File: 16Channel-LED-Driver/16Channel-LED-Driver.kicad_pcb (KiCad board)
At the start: 2 copper layers, 190.5 x 80 mm, 264 parts, among them P1 CONN_01X02, P10 CONN_01X02, P11 CONN_01X02, P12 CONN_01X02, P13 CONN_01X02, P14 CONN_01X02, P2 CONN_01X06, P3 CONN_01X02, P4 CONN_01X02, P5 CONN_01X06, P6 CONN_01X08, P7 CONN_01X08, P8 CONN_01X08, P9 CONN_01X08, Q1 BC413, Q10 BC413, Q11 BUT11, Q12 BC413, Q13 BUT11, Q14 BC413, Q15 BC413, Q16 BC413, Q17 BUT11, Q18 BC413, Q19 BC413, Q2 BC413, Q20 BC413, Q21 BUT11, Q22 BC413, Q23 BUT11, Q24 BC413, Q25 BUT11, Q26 BC413, Q27 BC413, Q28 BC413, Q29 BC413, Q3 BC413, Q30 BC413, Q31 BUT11, Q32 BC413, Q33 BUT11, Q34 BC413, Q35 BC413, Q36 BUT11, Q37 BC413, Q38 BUT11, Q4 BC413, Q5 BUT11, Q51 BC413, Q52 BC413, Q55 BC413, Q56 BUT11, Q57 BC413, Q58 BUT11, Q59 BC413, Q6 BC413, Q60 BC413, Q63 BC413, Q64 BUT11, Q65 BC413, Q66 BUT11, Q7 BUT11, Q8 BC413, Q9 BC413, U1 LD3985G, U2 LD3985G, U3 PCA9634, U4 LM324AN, U5 LM324AN, U6 PCA9634, U7 LM324AN, U8 LM324AN

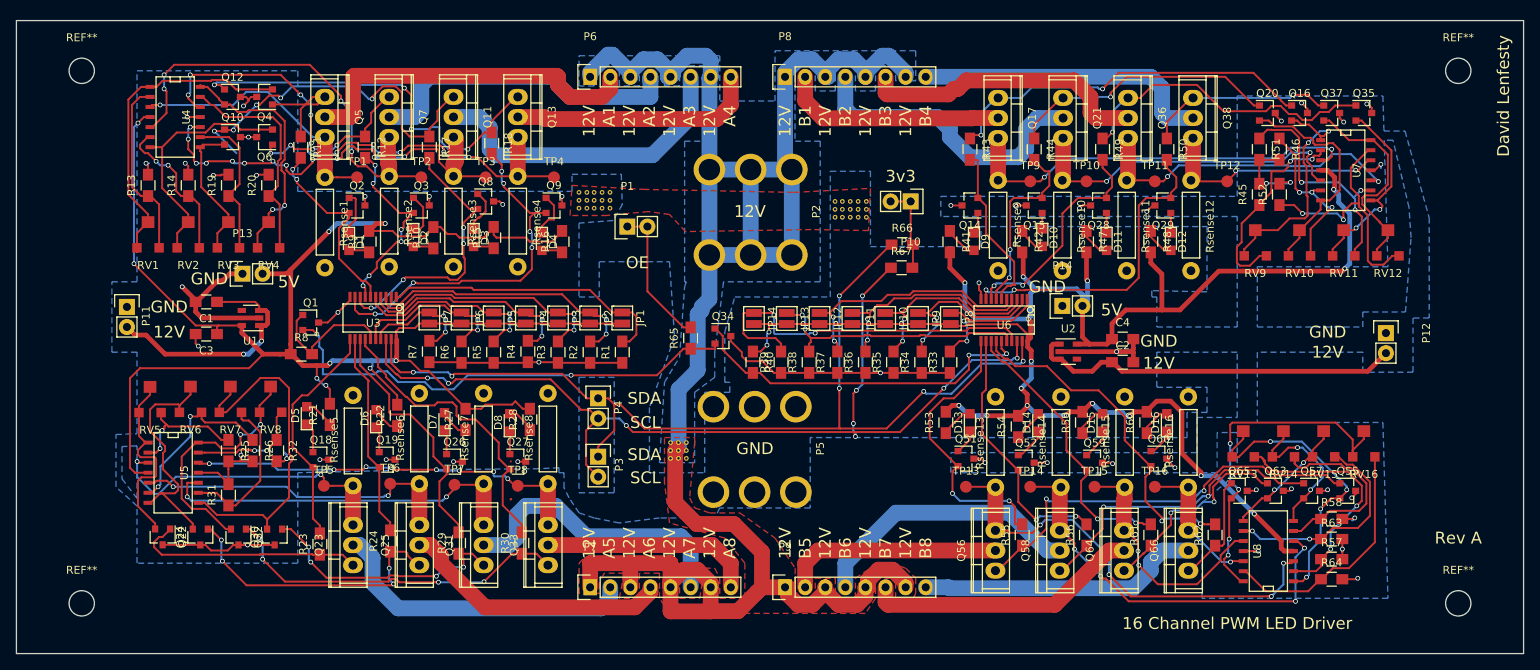
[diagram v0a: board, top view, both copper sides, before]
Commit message: Did Revision B of the 16 Channel board, also exported some gerbers
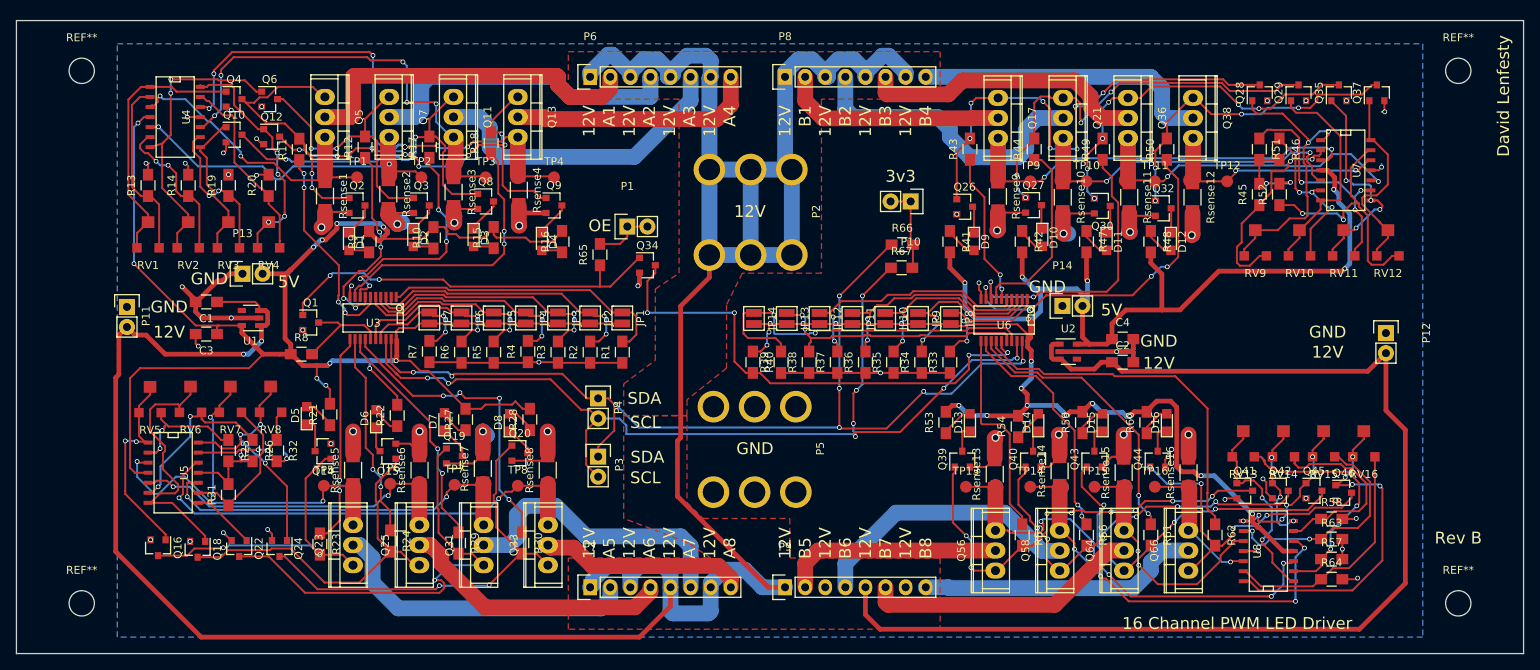
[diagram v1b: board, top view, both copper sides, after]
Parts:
- removed Q51, Q52, Q55, Q57, Q59, Q60, Q63, Q65: BC413, TO_SOT_Packages_SMD:SOT-23
- removed the REF** at (139.9, 105.4)
- removed the REF** at (138.9, 105.4)
- removed the REF** at (162.7, 76.9)
- removed the REF** at (162.7, 74.9)
- removed the REF** at (162.7, 75.9)
- removed the REF** at (161.6, 75.9)
- removed the REF** at (161.6, 76.9)
- removed the REF** at (160.6, 76.9)
- removed the REF** at (160.6, 75.9)
- removed the REF** at (158.7, 75.9)
- removed the REF** at (158.7, 76.9)
- removed the REF** at (159.6, 76.9)
- removed the REF** at (158.7, 74.9)
- removed the REF** at (159.6, 75.9)
- removed the REF** at (159.6, 74.9)
- removed the REF** at (161.6, 74.9)
- removed the REF** at (160.6, 74.9)
- removed the REF** at (126.3, 74.8)
- removed the REF** at (127.3, 75.8)
- removed the REF** at (127.3, 74.8)
- removed the REF** at (126.3, 75.8)
- removed the REF** at (126.3, 73.8)
- removed the REF** at (127.3, 73.8)
- removed the REF** at (130.3, 75.8)
- removed the REF** at (129.3, 75.8)
- removed the REF** at (128.3, 75.8)
- removed the REF** at (130.3, 74.8)
- removed the REF** at (129.3, 74.8)
- removed the REF** at (128.3, 74.8)
- removed the REF** at (130.3, 73.8)
- removed the REF** at (139.9, 107.4)
- removed the REF** at (129.3, 73.8)
- removed the REF** at (128.3, 73.8)
- removed the REF** at (137.9, 105.4)
- removed the REF** at (138.9, 107.4)
- removed the REF** at (137.9, 107.4)
- removed the REF** at (139.9, 106.4)
- removed the REF** at (138.9, 106.4)
- removed the REF** at (137.9, 106.4)
- added Q39: Q_NPN_BEC, TO_SOT_Packages_SMD:SOT-23, F.Cu at (174.8, 107.5)
- added Q40: Q_NPN_BEC, TO_SOT_Packages_SMD:SOT-23, F.Cu at (183.8, 107.5)
- added Q41: Q_NPN_BEC, TO_SOT_Packages_SMD:SOT-23, F.Cu at (210.5, 111.5)
- added Q42: Q_NPN_BEC, TO_SOT_Packages_SMD:SOT-23, F.Cu at (215.0, 111.5)
- added Q43: Q_NPN_BEC, TO_SOT_Packages_SMD:SOT-23, F.Cu at (191.5, 107.5)
- added Q44: Q_NPN_BEC, TO_SOT_Packages_SMD:SOT-23, F.Cu at (199.5, 107.5)
- added Q45: Q_NPN_BEC, TO_SOT_Packages_SMD:SOT-23, F.Cu at (219.2, 111.5)
- added Q46: Q_NPN_BEC, TO_SOT_Packages_SMD:SOT-23, F.Cu at (223.0, 111.8)
- Q1, Q10, Q12, Q14, Q15, Q16, Q18, Q19, Q2, Q20, Q22, Q24, Q26, Q27, Q28, Q29, Q3, Q30, Q32, Q34, Q35, Q37, Q4, Q6, Q8, Q9: value BC413 -> Q_NPN_BEC
- Rsense1, Rsense10, Rsense11, Rsense12, Rsense13, Rsense14, Rsense15, Rsense16, Rsense2, Rsense3, Rsense4, Rsense5, Rsense6, Rsense7, Rsense8, Rsense9: footprint Custom_Footprints:Current_Sense_Resistor -> Resistors_SMD:R_1206_HandSoldering
- moved Q16 154.4 mm to (73.2, 118.7), turned to 270 degrees
- moved Q32 124.1 mm to (200.2, 75.8), turned to 0 degrees
- moved Q30 112.7 mm to (192.5, 75.5), turned to 0 degrees
- moved Q20 103.8 mm to (118.9, 106.8)
- moved Q14 87.5 mm to (94.0, 106.5)
- moved Q15 87.4 mm to (102.2, 106.5)
- moved Q27 72.8 mm to (183.8, 75.4)
- moved Q26 72.1 mm to (175.1, 75.6)
- moved Q28 24.9 mm to (212.4, 61.2), turned to 90 degrees
- moved Q29 22.3 mm to (217.3, 61.2), turned to 90 degrees
- moved Q18 19.3 mm to (78.2, 118.9), turned to 270 degrees
- moved R65 15.6 mm to (129.0, 81.7)
- moved Q34 13.1 mm to (135.0, 83.0)
- moved Q24 10.1 mm to (88.5, 118.8)
- moved Q22 9.78 mm to (83.4, 118.8)
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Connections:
- C1 pad 1: /+12V-A -> +12V
- C2 pad 1: /+12V-B -> +12V
- P11 pad 2: /+12V-A -> +12V
- P12 pad 2: /+12V-B -> +12V
- Q1 pad 1: Net-(Q1-Pad1) -> OE-Disable
- Q1 pad 2: OE-Disable -> GND
- Q1 pad 3: GND -> Net-(Q1-Pad3)
- Q10 pad 2: Net-(Q10-Pad2) -> GND
- Q10 pad 3: GND -> Net-(Q10-Pad3)
- Q11 pad 1: Net-(Q10-Pad1) -> Net-(Q10-Pad3)
- Q12 pad 2: Net-(Q12-Pad2) -> GND
- Q12 pad 3: GND -> Net-(Q12-Pad3)
- Q13 pad 1: Net-(Q12-Pad1) -> Net-(Q12-Pad3)
- Q14 pad 1: Net-(D9-Pad1) -> Net-(Q14-Pad1)
- Q14 pad 2: /Power Driver B/LED Driver A/LED1 -> GND
- Q14 pad 3: GND -> Net-(D5-Pad1)
- Q15 pad 1: Net-(D10-Pad1) -> Net-(Q15-Pad1)
- Q15 pad 2: /Power Driver B/LED Driver A/LED2 -> GND
- Q15 pad 3: GND -> Net-(D6-Pad1)
- Q16 pad 2: Net-(Q16-Pad2) -> GND
- Q16 pad 3: GND -> Net-(Q14-Pad1)
- Q17 pad 1: Net-(Q16-Pad1) -> Net-(Q17-Pad1)
- Q18 pad 1: Net-(D5-Pad1) -> Net-(Q18-Pad1)
- Q18 pad 2: /Power Driver A/LED Driver B/LED1 -> GND
- Q18 pad 3: GND -> Net-(Q15-Pad1)
- Q19 pad 1: Net-(D6-Pad1) -> Net-(Q19-Pad1)
- Q19 pad 2: /Power Driver A/LED Driver B/LED2 -> GND
- Q19 pad 3: GND -> Net-(D7-Pad1)
- Q2 pad 1: Net-(D1-Pad1) -> Net-(Q2-Pad1)
- Q2 pad 2: /Power Driver A/LED Driver A/LED1 -> GND
- Q2 pad 3: GND -> Net-(D1-Pad1)
- Q20 pad 2: Net-(Q20-Pad2) -> GND
- Q20 pad 3: GND -> Net-(D8-Pad1)
- Q21 pad 1: Net-(Q20-Pad1) -> Net-(Q21-Pad1)
- Q22 pad 2: Net-(Q22-Pad2) -> GND
- Q22 pad 3: GND -> Net-(Q19-Pad1)
- Q23 pad 1: Net-(Q22-Pad1) -> Net-(Q14-Pad1)
- Q24 pad 2: Net-(Q24-Pad2) -> GND
- Q24 pad 3: GND -> Net-(Q20-Pad1)
- Q25 pad 1: Net-(Q24-Pad1) -> Net-(Q15-Pad1)
- Q26 pad 1: Net-(D7-Pad1) -> Net-(Q17-Pad1)
- Q26 pad 2: /Power Driver A/LED Driver B/LED3 -> GND
- Q26 pad 3: GND -> Net-(D9-Pad1)
- Q27 pad 1: Net-(D8-Pad1) -> Net-(Q21-Pad1)
- Q27 pad 2: /Power Driver A/LED Driver B/LED4 -> GND
- Q27 pad 3: GND -> Net-(D10-Pad1)
- Q28 pad 1: Net-(D11-Pad1) -> Net-(Q28-Pad1)
- Q28 pad 2: /Power Driver B/LED Driver A/LED3 -> GND
- Q28 pad 3: GND -> Net-(Q17-Pad1)
- Q29 pad 1: Net-(D12-Pad1) -> Net-(Q29-Pad1)
- Q29 pad 2: /Power Driver B/LED Driver A/LED4 -> GND
- Q29 pad 3: GND -> Net-(Q21-Pad1)
- Q3 pad 1: Net-(D2-Pad1) -> Net-(Q3-Pad1)
- Q3 pad 2: /Power Driver A/LED Driver A/LED2 -> GND
- Q3 pad 3: GND -> Net-(D2-Pad1)
- Q30 pad 2: Net-(Q30-Pad2) -> GND
- Q30 pad 3: GND -> Net-(D11-Pad1)
- Q31 pad 1: Net-(Q30-Pad1) -> Net-(Q19-Pad1)
- Q32 pad 2: Net-(Q32-Pad2) -> GND
- Q32 pad 3: GND -> Net-(D12-Pad1)
- Q33 pad 1: Net-(Q32-Pad1) -> Net-(Q20-Pad1)
- Q34 pad 1: Net-(Q34-Pad1) -> OE-Disable
- Q34 pad 2: OE-Disable -> GND
- Q34 pad 3: GND -> Net-(Q34-Pad3)
- Q35 pad 2: Net-(Q35-Pad2) -> GND
- Q35 pad 3: GND -> Net-(Q30-Pad1)
- Q36 pad 1: Net-(Q35-Pad1) -> Net-(Q30-Pad1)
- Q37 pad 2: Net-(Q37-Pad2) -> GND
- Q37 pad 3: GND -> Net-(Q32-Pad1)
- Q38 pad 1: Net-(Q37-Pad1) -> Net-(Q32-Pad1)
- Q4 pad 2: Net-(Q4-Pad2) -> GND
- Q4 pad 3: GND -> Net-(Q2-Pad1)
- Q5 pad 1: Net-(Q4-Pad1) -> Net-(Q2-Pad1)
- Q56 pad 1: Net-(Q55-Pad1) -> Net-(Q39-Pad1)
- Q58 pad 1: Net-(Q57-Pad1) -> Net-(Q40-Pad1)
- Q6 pad 2: Net-(Q6-Pad2) -> GND
- Q6 pad 3: GND -> Net-(Q3-Pad1)
- Q64 pad 1: Net-(Q63-Pad1) -> Net-(Q43-Pad1)
- Q66 pad 1: Net-(Q65-Pad1) -> Net-(Q44-Pad1)
- Q7 pad 1: Net-(Q6-Pad1) -> Net-(Q3-Pad1)
- Q8 pad 1: Net-(D3-Pad1) -> Net-(Q10-Pad3)
- Q8 pad 2: /Power Driver A/LED Driver A/LED3 -> GND
- Q8 pad 3: GND -> Net-(D3-Pad1)
- Q9 pad 1: Net-(D4-Pad1) -> Net-(Q12-Pad3)
- Q9 pad 2: /Power Driver A/LED Driver A/LED4 -> GND
- Q9 pad 3: GND -> Net-(D4-Pad1)
- R11 pad 1: Net-(Q4-Pad1) -> /Power Driver A/LED Driver A/LED1
- R11 pad 2: /Power Driver A/LED Driver A/LED1 -> Net-(Q2-Pad1)
- R12 pad 1: Net-(Q6-Pad1) -> /Power Driver A/LED Driver A/LED2
- R12 pad 2: /Power Driver A/LED Driver A/LED2 -> Net-(Q3-Pad1)
- R17 pad 1: Net-(Q10-Pad1) -> /Power Driver A/LED Driver A/LED3
- R17 pad 2: /Power Driver A/LED Driver A/LED3 -> Net-(Q10-Pad3)
- R18 pad 1: Net-(Q12-Pad1) -> /Power Driver A/LED Driver A/LED4
- R18 pad 2: /Power Driver A/LED Driver A/LED4 -> Net-(Q12-Pad3)
- R23 pad 1: Net-(Q22-Pad1) -> /Power Driver A/LED Driver B/LED1
- R23 pad 2: /Power Driver A/LED Driver B/LED1 -> Net-(Q14-Pad1)
- R24 pad 1: Net-(Q24-Pad1) -> /Power Driver A/LED Driver B/LED2
- R24 pad 2: /Power Driver A/LED Driver B/LED2 -> Net-(Q15-Pad1)
- R29 pad 1: Net-(Q30-Pad1) -> /Power Driver A/LED Driver B/LED3
- R29 pad 2: /Power Driver A/LED Driver B/LED3 -> Net-(Q19-Pad1)
- R30 pad 1: Net-(Q32-Pad1) -> /Power Driver A/LED Driver B/LED4
- R30 pad 2: /Power Driver A/LED Driver B/LED4 -> Net-(Q20-Pad1)
- R40 pad 2: Net-(Q34-Pad1) -> Net-(Q34-Pad3)
- R43 pad 1: Net-(Q16-Pad1) -> /Power Driver B/LED Driver A/LED1
- R43 pad 2: /Power Driver B/LED Driver A/LED1 -> Net-(Q17-Pad1)
- R44 pad 1: Net-(Q20-Pad1) -> /Power Driver B/LED Driver A/LED2
- R44 pad 2: /Power Driver B/LED Driver A/LED2 -> Net-(Q21-Pad1)
- R49 pad 1: Net-(Q35-Pad1) -> /Power Driver B/LED Driver A/LED3
- R49 pad 2: /Power Driver B/LED Driver A/LED3 -> Net-(Q30-Pad1)
- R50 pad 1: Net-(Q37-Pad1) -> /Power Driver B/LED Driver A/LED4
- R50 pad 2: /Power Driver B/LED Driver A/LED4 -> Net-(Q32-Pad1)
- R55 pad 1: Net-(Q55-Pad1) -> /Power Driver B/LED Driver B/LED1
- R55 pad 2: /Power Driver B/LED Driver B/LED1 -> Net-(Q39-Pad1)
- R56 pad 1: Net-(Q57-Pad1) -> /Power Driver B/LED Driver B/LED2
- R56 pad 2: /Power Driver B/LED Driver B/LED2 -> Net-(Q40-Pad1)
- R61 pad 1: Net-(Q63-Pad1) -> /Power Driver B/LED Driver B/LED3
- R61 pad 2: /Power Driver B/LED Driver B/LED3 -> Net-(Q43-Pad1)
- R62 pad 1: Net-(Q65-Pad1) -> /Power Driver B/LED Driver B/LED4
- R62 pad 2: /Power Driver B/LED Driver B/LED4 -> Net-(Q44-Pad1)
- R8 pad 2: Net-(Q1-Pad1) -> Net-(Q1-Pad3)
- RV1 pad 1: Net-(Q4-Pad2) -> Net-(Q4-Pad1)
- RV1 pad 2: Net-(Q4-Pad2) -> Net-(Q4-Pad1)
- RV10 pad 1: Net-(Q20-Pad2) -> Net-(Q29-Pad1)
- RV10 pad 2: Net-(Q20-Pad2) -> Net-(Q29-Pad1)
- RV11 pad 1: Net-(Q35-Pad2) -> Net-(Q35-Pad1)
- RV11 pad 2: Net-(Q35-Pad2) -> Net-(Q35-Pad1)
- RV12 pad 1: Net-(Q37-Pad2) -> Net-(Q37-Pad1)
- RV12 pad 2: Net-(Q37-Pad2) -> Net-(Q37-Pad1)
- RV2 pad 1: Net-(Q6-Pad2) -> Net-(Q6-Pad1)
- RV2 pad 2: Net-(Q6-Pad2) -> Net-(Q6-Pad1)
- RV3 pad 1: Net-(Q10-Pad2) -> Net-(Q10-Pad1)
- RV3 pad 2: Net-(Q10-Pad2) -> Net-(Q10-Pad1)
- RV4 pad 1: Net-(Q12-Pad2) -> Net-(Q12-Pad1)
- RV4 pad 2: Net-(Q12-Pad2) -> Net-(Q12-Pad1)
- RV5 pad 1: Net-(Q22-Pad2) -> Net-(Q16-Pad1)
- RV5 pad 2: Net-(Q22-Pad2) -> Net-(Q16-Pad1)
- RV6 pad 1: Net-(Q24-Pad2) -> Net-(Q18-Pad1)
- RV6 pad 2: Net-(Q24-Pad2) -> Net-(Q18-Pad1)
- RV7 pad 1: Net-(Q30-Pad2) -> Net-(Q22-Pad1)
- RV7 pad 2: Net-(Q30-Pad2) -> Net-(Q22-Pad1)
- RV8 pad 1: Net-(Q32-Pad2) -> Net-(Q24-Pad1)
- RV8 pad 2: Net-(Q32-Pad2) -> Net-(Q24-Pad1)
- RV9 pad 1: Net-(Q16-Pad2) -> Net-(Q28-Pad1)
- RV9 pad 2: Net-(Q16-Pad2) -> Net-(Q28-Pad1)
- U1 pad 1: /+12V-A -> +12V
- U1 pad 3: /+12V-A -> +12V
- U2 pad 1: /+12V-B -> +12V
- U2 pad 3: /+12V-B -> +12V
- U3 pad 15: Net-(Q1-Pad1) -> Net-(Q1-Pad3)
- U4 pad 1: Net-(Q4-Pad2) -> Net-(Q4-Pad1)
- U4 pad 14: Net-(Q12-Pad2) -> Net-(Q12-Pad1)
- U4 pad 7: Net-(Q6-Pad2) -> Net-(Q6-Pad1)
- U4 pad 8: Net-(Q10-Pad2) -> Net-(Q10-Pad1)
- U5 pad 1: Net-(Q22-Pad2) -> Net-(Q16-Pad1)
- U5 pad 14: Net-(Q32-Pad2) -> Net-(Q24-Pad1)
- U5 pad 7: Net-(Q24-Pad2) -> Net-(Q18-Pad1)
- U5 pad 8: Net-(Q30-Pad2) -> Net-(Q22-Pad1)
- U6 pad 15: Net-(Q34-Pad1) -> Net-(Q34-Pad3)
- U7 pad 1: Net-(Q16-Pad2) -> Net-(Q28-Pad1)
- U7 pad 14: Net-(Q37-Pad2) -> Net-(Q37-Pad1)
- U7 pad 7: Net-(Q20-Pad2) -> Net-(Q29-Pad1)
- U7 pad 8: Net-(Q35-Pad2) -> Net-(Q35-Pad1)
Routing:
- net +12V: track 249.2 -> 506.8 mm, vias 0 -> 2
- net Net-(Q34-Pad3): track 0.00 -> 63.9 mm, vias 0 -> 4
- net Net-(Q17-Pad1): track 0.00 -> 63.5 mm, vias 0 -> 7
- net Net-(Q19-Pad1): track 0.00 -> 55.7 mm, vias 0 -> 1
- net Net-(Q39-Pad1): track 0.00 -> 55.6 mm, vias 0 -> 8
- net Net-(Q12-Pad3): track 0.00 -> 53.1 mm, vias 0 -> 8
- net Net-(Q21-Pad1): track 0.00 -> 53.0 mm, vias 0 -> 4
- net Net-(Q55-Pad1): track 52.7 -> 0.00 mm, vias 2 -> 0
- net Net-(Q40-Pad1): track 0.00 -> 50.1 mm, vias 0 -> 6
- net /+12V-B: track 47.5 -> 0.00 mm
- net Net-(Q10-Pad3): track 0.00 -> 46.8 mm, vias 0 -> 2
- net Net-(Q43-Pad1): track 0.00 -> 46.5 mm, vias 0 -> 3
- net Net-(Q15-Pad1): track 0.00 -> 45.5 mm
- net Net-(Q34-Pad1): track 45.3 -> 0.00 mm, vias 2 -> 0
- net Net-(Q30-Pad2): track 43.8 -> 0.00 mm
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- removed copper zone on B.Cu, net +12V
- removed copper zone on F.Cu, net GND
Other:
- board text added: "Rev B"
- board text removed: "Rev A"

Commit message: Did third and hopefully final revision of the 16 channel LED board. I like making dumb mistakes. :(
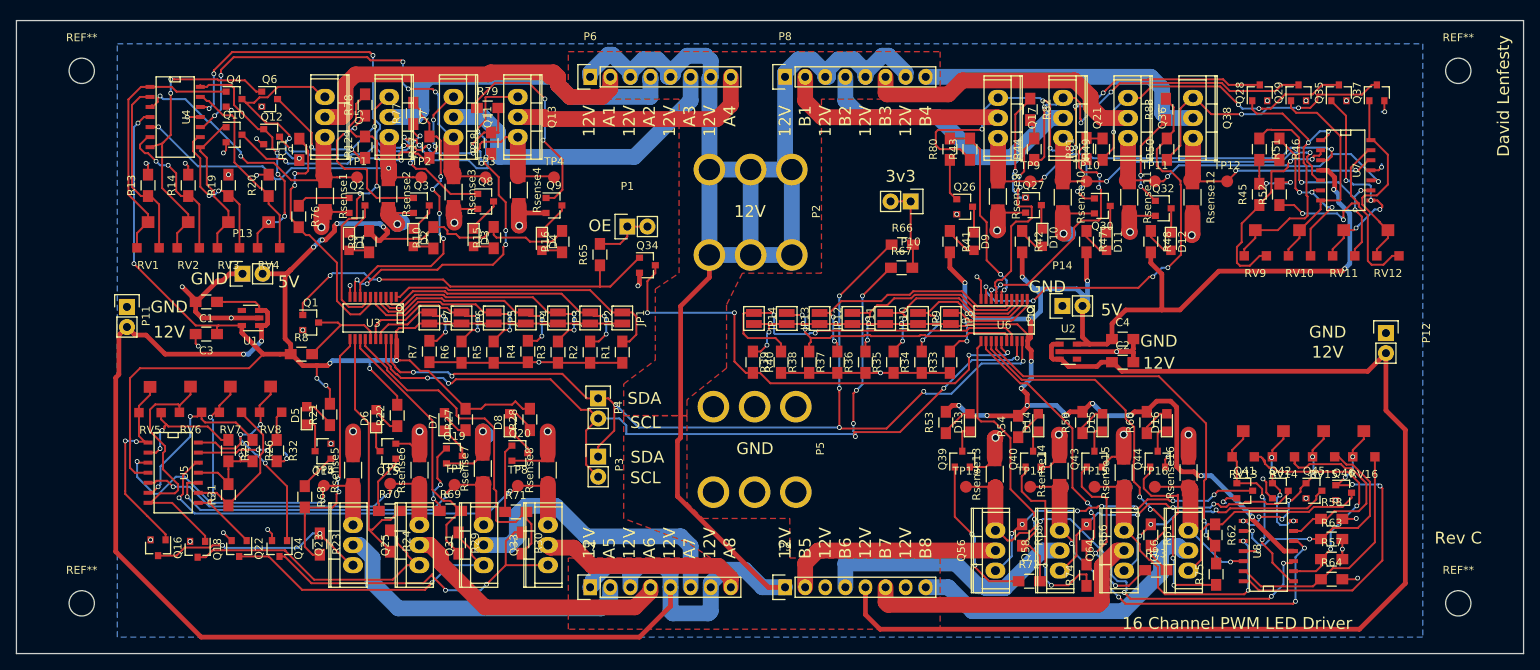
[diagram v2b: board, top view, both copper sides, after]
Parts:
- added R68: 10K, Resistors_SMD:R_0805_HandSoldering, F.Cu at (91.7, 112.3)
- added R69: 10K, Resistors_SMD:R_0805_HandSoldering, F.Cu at (110.1, 114.0)
- added R70: 10K, Resistors_SMD:R_0805_HandSoldering, F.Cu at (102.4, 114.0)
- added R71: 10K, Resistors_SMD:R_0805_HandSoldering, F.Cu at (118.4, 114.2)
- added R72: 10K, Resistors_SMD:R_0805_HandSoldering, F.Cu at (183.3, 122.9)
- added R73: 10K, Resistors_SMD:R_0805_HandSoldering, F.Cu at (199.3, 121.5)
- added R74: 10K, Resistors_SMD:R_0805_HandSoldering, F.Cu at (190.5, 122.2)
- added R75: 10K, Resistors_SMD:R_0805_HandSoldering, F.Cu at (206.9, 122.0)
- added R76: 10K, Resistors_SMD:R_0805_HandSoldering, F.Cu at (90.9, 76.8)
- added R77: 10K, Resistors_SMD:R_0805_HandSoldering, F.Cu at (105.4, 63.8)
- added R78: 10K, Resistors_SMD:R_0805_HandSoldering, F.Cu at (99.3, 62.7)
- added R79: 10K, Resistors_SMD:R_0805_HandSoldering, F.Cu at (114.8, 63.1)
- added R80: 10K, Resistors_SMD:R_0805_HandSoldering, F.Cu at (173.2, 68.3)
- added R81: 10K, Resistors_SMD:R_0805_HandSoldering, F.Cu at (190.5, 68.2)
- added R82: 10K, Resistors_SMD:R_0805_HandSoldering, F.Cu at (183.4, 63.3)
- added R83: 10K, Resistors_SMD:R_0805_HandSoldering, F.Cu at (200.5, 63.3)
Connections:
- Q16 pad 3: Net-(Q14-Pad1) -> Net-(Q16-Pad3)
- Q18 pad 3: Net-(Q15-Pad1) -> Net-(Q18-Pad3)
- Q22 pad 3: Net-(Q19-Pad1) -> Net-(Q22-Pad3)
- Q23 pad 1: Net-(Q14-Pad1) -> Net-(Q16-Pad3)
- Q24 pad 3: Net-(Q20-Pad1) -> Net-(Q24-Pad3)
- Q25 pad 1: Net-(Q15-Pad1) -> Net-(Q18-Pad3)
- Q26 pad 1: Net-(Q17-Pad1) -> Net-(Q26-Pad1)
- Q27 pad 1: Net-(Q21-Pad1) -> Net-(Q27-Pad1)
- Q31 pad 1: Net-(Q19-Pad1) -> Net-(Q22-Pad3)
- Q33 pad 1: Net-(Q20-Pad1) -> Net-(Q24-Pad3)
- Q35 pad 3: Net-(Q30-Pad1) -> Net-(Q35-Pad3)
- Q36 pad 1: Net-(Q30-Pad1) -> Net-(Q35-Pad3)
- Q37 pad 3: Net-(Q32-Pad1) -> Net-(Q37-Pad3)
- Q38 pad 1: Net-(Q32-Pad1) -> Net-(Q37-Pad3)
- Q4 pad 3: Net-(Q2-Pad1) -> Net-(Q4-Pad3)
- Q41 pad 3: Net-(Q39-Pad1) -> Net-(Q41-Pad3)
- Q42 pad 3: Net-(Q40-Pad1) -> Net-(Q42-Pad3)
- Q45 pad 3: Net-(Q43-Pad1) -> Net-(Q45-Pad3)
- Q46 pad 3: Net-(Q44-Pad1) -> Net-(Q46-Pad3)
- Q5 pad 1: Net-(Q2-Pad1) -> Net-(Q4-Pad3)
- Q56 pad 1: Net-(Q39-Pad1) -> Net-(Q41-Pad3)
- Q58 pad 1: Net-(Q40-Pad1) -> Net-(Q42-Pad3)
- Q6 pad 3: Net-(Q3-Pad1) -> Net-(Q6-Pad3)
- Q64 pad 1: Net-(Q43-Pad1) -> Net-(Q45-Pad3)
- Q66 pad 1: Net-(Q44-Pad1) -> Net-(Q46-Pad3)
- Q7 pad 1: Net-(Q3-Pad1) -> Net-(Q6-Pad3)
- Q8 pad 1: Net-(Q10-Pad3) -> Net-(Q8-Pad1)
- Q9 pad 1: Net-(Q12-Pad3) -> Net-(Q9-Pad1)
- R11 pad 1: /Power Driver A/LED Driver A/LED1 -> Net-(Q4-Pad3)
- R11 pad 2: Net-(Q2-Pad1) -> /Power Driver A/LED Driver A/LED1
- R12 pad 1: /Power Driver A/LED Driver A/LED2 -> Net-(Q6-Pad3)
- R12 pad 2: Net-(Q3-Pad1) -> /Power Driver A/LED Driver A/LED2
- R17 pad 1: /Power Driver A/LED Driver A/LED3 -> Net-(Q10-Pad3)
- R17 pad 2: Net-(Q10-Pad3) -> /Power Driver A/LED Driver A/LED3
- R18 pad 1: /Power Driver A/LED Driver A/LED4 -> Net-(Q12-Pad3)
- R18 pad 2: Net-(Q12-Pad3) -> /Power Driver A/LED Driver A/LED4
- R23 pad 1: /Power Driver A/LED Driver B/LED1 -> Net-(Q16-Pad3)
- R23 pad 2: Net-(Q14-Pad1) -> /Power Driver A/LED Driver B/LED1
- R24 pad 1: /Power Driver A/LED Driver B/LED2 -> Net-(Q18-Pad3)
- R24 pad 2: Net-(Q15-Pad1) -> /Power Driver A/LED Driver B/LED2
- R29 pad 1: /Power Driver A/LED Driver B/LED3 -> Net-(Q22-Pad3)
- R29 pad 2: Net-(Q19-Pad1) -> /Power Driver A/LED Driver B/LED3
- R30 pad 1: /Power Driver A/LED Driver B/LED4 -> Net-(Q24-Pad3)
- R30 pad 2: Net-(Q20-Pad1) -> /Power Driver A/LED Driver B/LED4
- R43 pad 1: /Power Driver B/LED Driver A/LED1 -> Net-(Q17-Pad1)
- R43 pad 2: Net-(Q17-Pad1) -> /Power Driver B/LED Driver A/LED1
- R44 pad 1: /Power Driver B/LED Driver A/LED2 -> Net-(Q21-Pad1)
- R44 pad 2: Net-(Q21-Pad1) -> /Power Driver B/LED Driver A/LED2
- R49 pad 1: /Power Driver B/LED Driver A/LED3 -> Net-(Q35-Pad3)
- R49 pad 2: Net-(Q30-Pad1) -> /Power Driver B/LED Driver A/LED3
- R50 pad 1: /Power Driver B/LED Driver A/LED4 -> Net-(Q37-Pad3)
- R50 pad 2: Net-(Q32-Pad1) -> /Power Driver B/LED Driver A/LED4
- R55 pad 1: /Power Driver B/LED Driver B/LED1 -> Net-(Q41-Pad3)
- R55 pad 2: Net-(Q39-Pad1) -> /Power Driver B/LED Driver B/LED1
- R56 pad 1: /Power Driver B/LED Driver B/LED2 -> Net-(Q42-Pad3)
- R56 pad 2: Net-(Q40-Pad1) -> /Power Driver B/LED Driver B/LED2
- R61 pad 1: /Power Driver B/LED Driver B/LED3 -> Net-(Q45-Pad3)
- R61 pad 2: Net-(Q43-Pad1) -> /Power Driver B/LED Driver B/LED3
- R62 pad 1: /Power Driver B/LED Driver B/LED4 -> Net-(Q46-Pad3)
- R62 pad 2: Net-(Q44-Pad1) -> /Power Driver B/LED Driver B/LED4
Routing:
- net Net-(Q19-Pad1): track 55.7 -> 9.26 mm, vias 1 -> 2
- net Net-(Q20-Pad1): track 54.2 -> 8.76 mm, vias 2 -> 0
- net Net-(Q24-Pad3): track 0.00 -> 43.7 mm, vias 0 -> 2
- net Net-(Q41-Pad3): track 0.00 -> 39.7 mm, vias 0 -> 7
- net Net-(Q30-Pad1): track 46.7 -> 7.05 mm, vias 6 -> 2
- net Net-(Q22-Pad3): track 0.00 -> 39.5 mm, vias 0 -> 1
- net Net-(Q35-Pad3): track 0.00 -> 39.0 mm, vias 0 -> 3
- net Net-(Q15-Pad1): track 45.5 -> 7.56 mm
- net Net-(Q18-Pad3): track 0.00 -> 37.6 mm
- net Net-(Q42-Pad3): track 0.00 -> 36.9 mm, vias 0 -> 4
- net Net-(Q14-Pad1): track 40.8 -> 4.87 mm, vias 2 -> 0
- net Net-(Q39-Pad1): track 55.6 -> 20.0 mm, vias 8 -> 2
- net Net-(Q37-Pad3): track 0.00 -> 35.4 mm, vias 0 -> 2
- net Net-(Q45-Pad3): track 0.00 -> 32.2 mm, vias 0 -> 3
- net Net-(Q32-Pad1): track 41.2 -> 12.3 mm, vias 4 -> 2
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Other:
- board text added: "Rev C"
- board text removed: "Rev B"
